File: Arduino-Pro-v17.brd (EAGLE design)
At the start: 100 x 80 mm, 35 parts, among them IC1 ATMEGA1281-16AU, IC2 MCP170312MB, J1 FTDI Basic Programmer

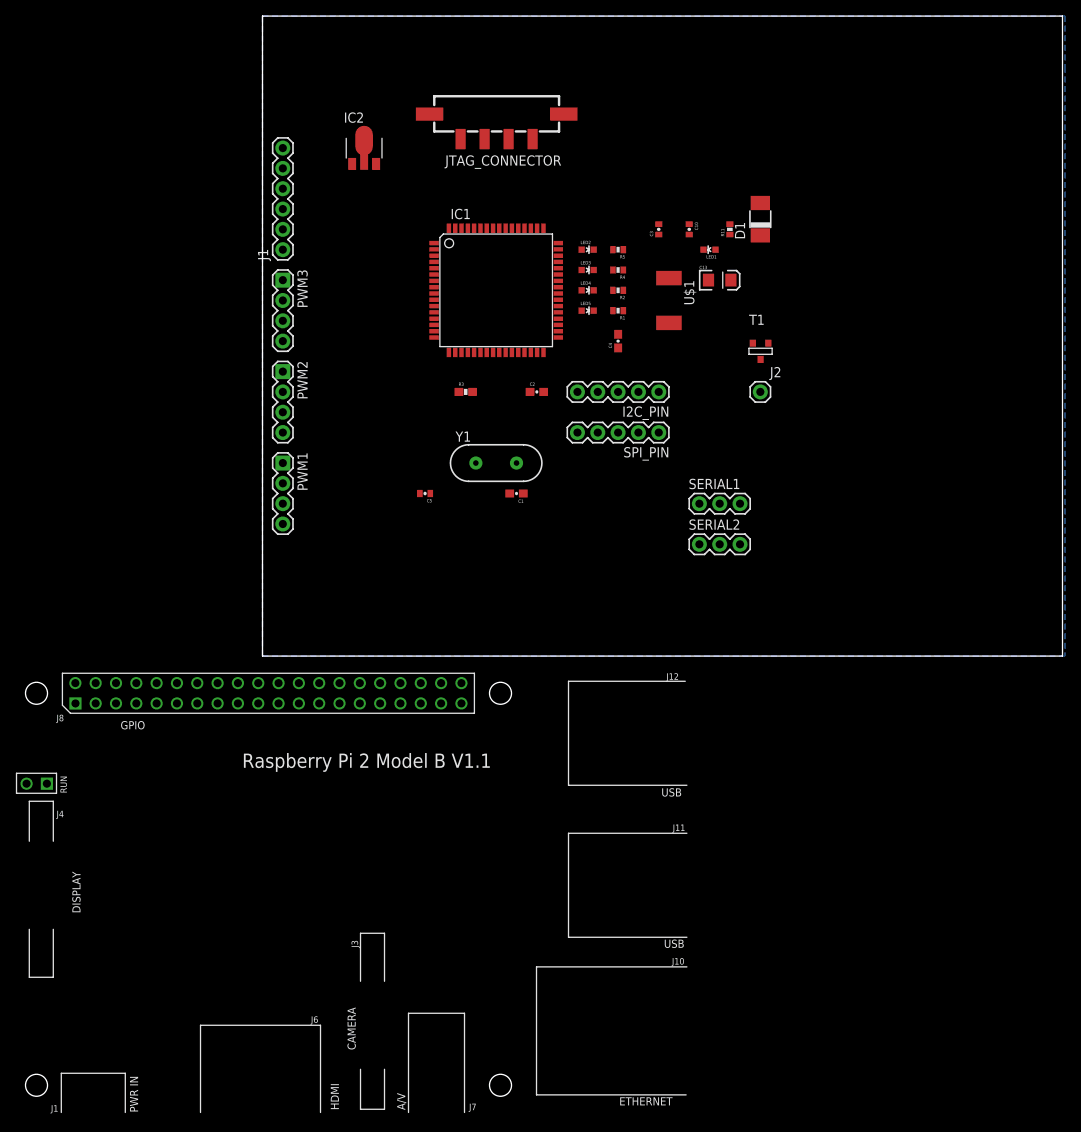
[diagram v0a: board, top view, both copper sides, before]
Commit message: Added extra pinouts for JTAG, continued with layout
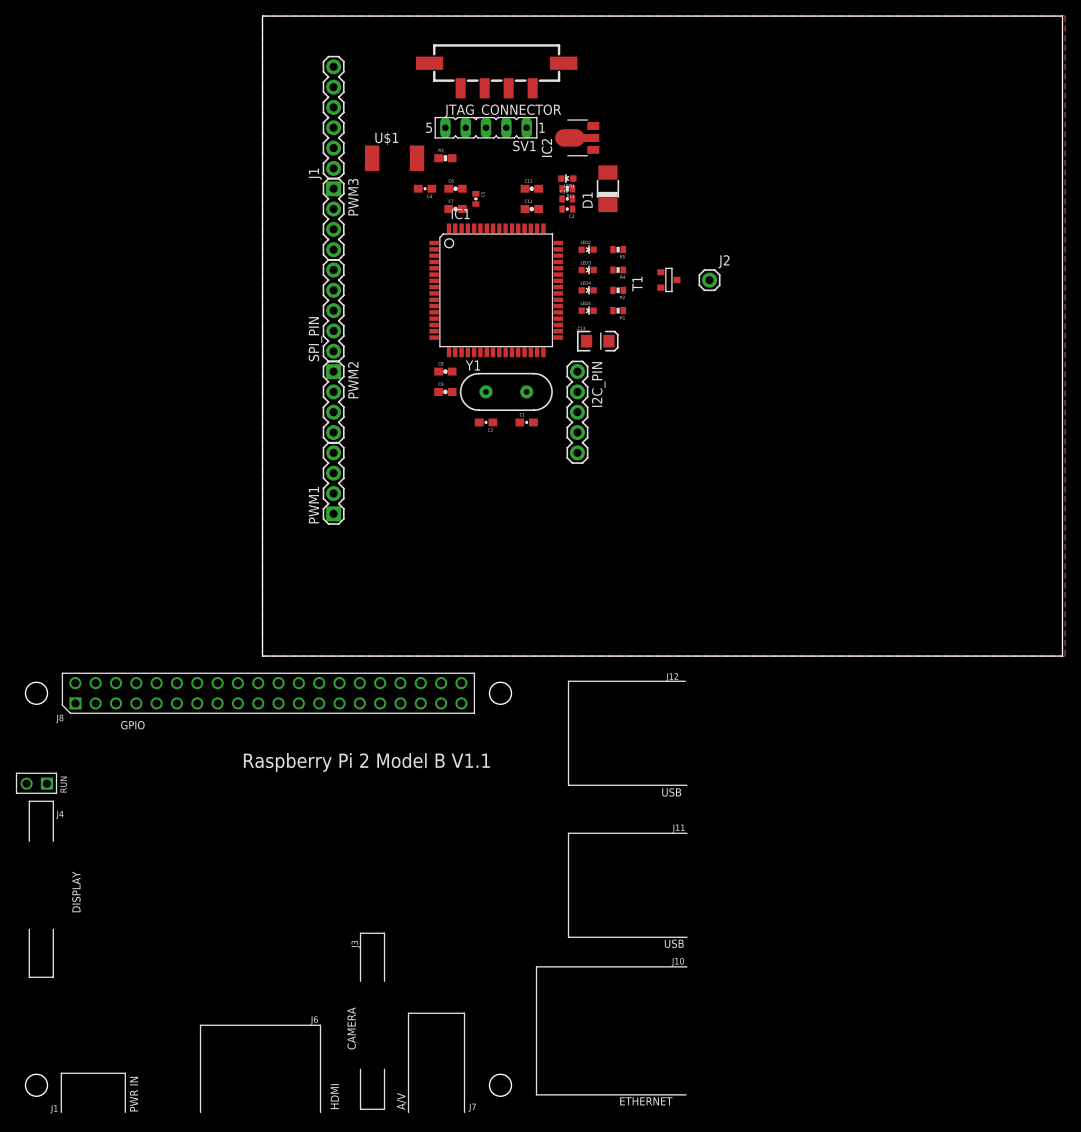
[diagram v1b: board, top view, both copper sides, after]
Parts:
- removed SERIAL1, SERIAL2: (no value), SparkFun-Connectors:1X03
- added C11, C12, C6, C7, C8, C9: 10uF, SparkFun-Passives:0603-CAP
- added SV1: (no value), con-lsta:FE05-1
- moved SPI_PIN 41.9 mm to (8.89, 38.1), turned to 90 degrees
- moved U$1 38.6 mm to (16.5, 62.2), turned to 0 degrees
- moved C5 37.4 mm to (26.7, 57.1), turned to 270 degrees
- moved C4 30.7 mm to (20.3, 58.4), turned to 180 degrees
- moved R3 29.3 mm to (22.9, 62.2)
- moved IC2 26.7 mm to (39.4, 64.8), turned to 90 degrees
- moved R11 20.9 mm to (38.1, 58.4), turned to 180 degrees
- moved LED1 19.9 mm to (38.1, 59.7)
- moved D1 19.4 mm to (43.2, 58.4)
- moved C13 17.0 mm to (41.9, 39.4)
- moved C10 15.7 mm to (38.1, 57.1), turned to 0 degrees
- moved J2 15.3 mm to (55.9, 47.0)
- moved T1 14.5 mm to (50.8, 47.0), turned to 90 degrees
- moved PWM3 13.1 mm to (8.89, 58.4)
- moved J1 12.0 mm to (8.89, 61.0)
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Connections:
- removed net N$2: SERIAL1.1
- removed net N$4: SERIAL1.2
- removed net N$6: SERIAL2.1
- removed net N$8: SERIAL2.2
- net GND: now also C11.2, C12.2, C6.2, C7.2, C8.2, C9.2, SV1.5; no longer SERIAL1.3, SERIAL2.3
- net JTTCK: now also SV1.4
- net JTTDI: now also SV1.1
- net JTTDO: now also SV1.2
- net JTTMS: now also SV1.3
- net MISO: now also IC1.13
- net MOSI: now also IC1.12
- net SCK: now also IC1.11
- net VCC: now also C11.1, C12.1, C6.1, C7.1, C8.1, C9.1
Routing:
- added copper zone on layer 1, net GND
- removed copper zone on layer 16, net GND
